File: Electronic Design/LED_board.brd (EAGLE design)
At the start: 49.2 x 29.2 mm, 12 parts

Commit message: Adding resistor values
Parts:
- R1, R2, R3, R4, R5: value (none) -> 270E
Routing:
- net N$3: track 27.1 -> 25.6 mm
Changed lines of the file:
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@@
 <attribute name="VALUE" x="6.8834" y="26.0604" size="1.27" layer="27" ratio="10" rot="R90"/>
 </element>
-<element name="R1" library="resistor" package="R0805" value="" x="35.56" y="7.62"/>
-<element name="R2" library="resistor" package="R0805" value="" x="35.56" y="15.24"/>
-<element name="R3" library="resistor" package="R0805" value="" x="35.56" y="22.86"/>
-<element name="R4" library="resistor" package="R0805" value="" x="20.32" y="16.51" rot="R90"/>
-<element name="R5" library="resistor" package="R0805" value="" x="12.7" y="16.51" rot="R90"/>
+<element name="R1" library="resistor" package="R0805" value="270E" x="35.56" y="7.62"/>
+<element name="R2" library="resistor" package="R0805" value="270E" x="35.56" y="15.24"/>
+<element name="R3" library="resistor" package="R0805" value="270E" x="35.56" y="22.86"/>
+<element name="R4" library="resistor" package="R0805" value="270E" x="20.32" y="16.51" rot="R90"/>
+<element name="R5" library="resistor" package="R0805" value="270E" x="12.7" y="16.51" rot="R90"/>
 </elements>
 <signals>
@@
 <contactref element="R3" pad="1"/>
 <contactref element="JP1" pad="3"/>
-<wire x1="22.86" y1="3.81" x2="22.86" y2="16.51" width="0.8128" layer="1"/>
-<wire x1="22.86" y1="16.51" x2="29.21" y2="22.86" width="0.8128" layer="1"/>
-<wire x1="29.21" y1="22.86" x2="34.61" y2="22.86" width="0.8128" layer="1"/>
+<wire x1="22.86" y1="3.81" x2="22.86" y2="13.97" width="0.8128" layer="1"/>
+<wire x1="22.86" y1="13.97" x2="31.75" y2="22.86" width="0.8128" layer="1"/>
+<wire x1="31.75" y1="22.86" x2="34.61" y2="22.86" width="0.8128" layer="1"/>
 </signal>
 <signal name="N$5">

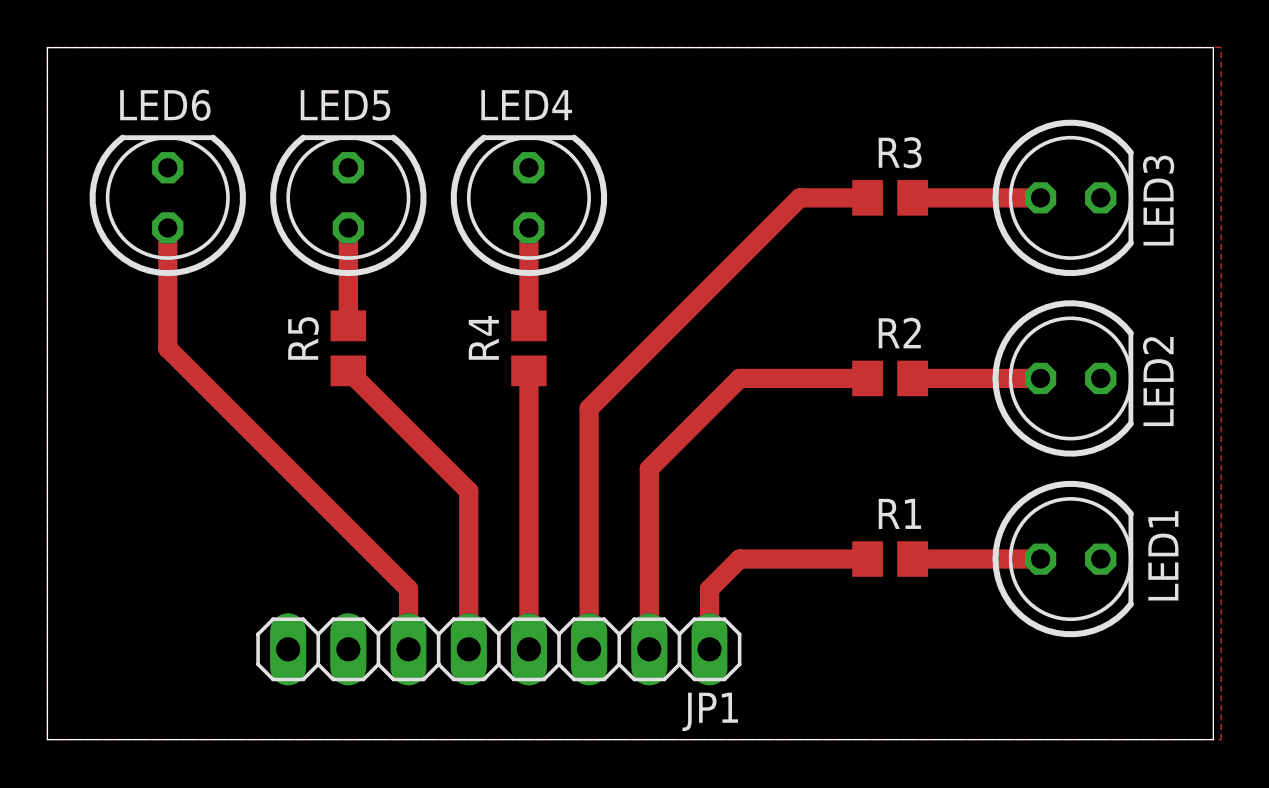
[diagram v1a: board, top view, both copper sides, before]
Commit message: added drill holes
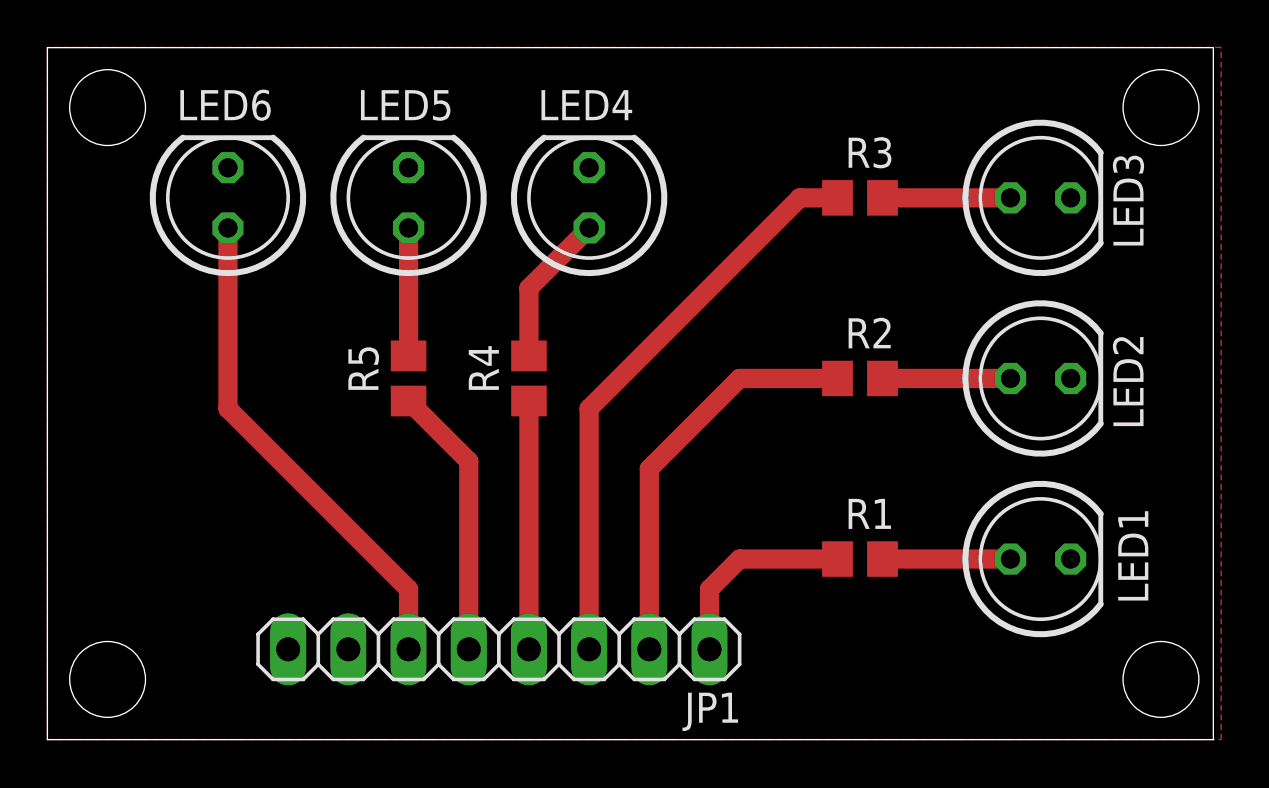
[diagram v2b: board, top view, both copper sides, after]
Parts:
- moved R5 2.84 mm to (15.2, 15.2)
- moved LED5 2.54 mm to (15.2, 22.9)
- moved LED6 2.54 mm to (7.62, 22.9)
- moved LED4 2.54 mm to (22.9, 22.9)
- moved LED1 1.27 mm to (41.9, 7.62)
- moved LED2 1.27 mm to (41.9, 15.2)
- moved LED3 1.27 mm to (41.9, 22.9)
- moved R1 1.27 mm to (34.3, 7.62)
- moved R2 1.27 mm to (34.3, 15.2)
- moved R3 1.27 mm to (34.3, 22.9)
- moved R4 1.27 mm to (20.3, 15.2)
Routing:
- net N$6: track 13.9 -> 11.5 mm
- net N$8: track 4.13 -> 6.45 mm
- net N$4: track 11.8 -> 10.5 mm
- net N$7: track 4.13 -> 5.40 mm
- net N$3: track 25.6 -> 24.3 mm
- net N$2: track 18.4 -> 17.1 mm
- net N$1: track 9.74 -> 8.47 mm
- net N$5: track 22.0 -> 20.9 mm
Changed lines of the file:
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@@
 <layer number="43" name="vRestrict" color="2" fill="10" visible="yes" active="yes"/>
 <layer number="44" name="Drills" color="7" fill="1" visible="no" active="yes"/>
-<layer number="45" name="Holes" color="7" fill="1" visible="no" active="yes"/>
+<layer number="45" name="Holes" color="7" fill="1" visible="yes" active="yes"/>
 <layer number="46" name="Milling" color="3" fill="1" visible="no" active="yes"/>
 <layer number="47" name="Measures" color="7" fill="1" visible="no" active="yes"/>
@@
 <wire x1="49.2" y1="29.2" x2="0" y2="29.2" width="0" layer="20"/>
 <wire x1="0" y1="29.2" x2="0" y2="0" width="0" layer="20"/>
+<hole x="46.99" y="26.67" drill="3.2"/>
+<hole x="46.99" y="2.54" drill="3.2"/>
+<hole x="2.54" y="2.54" drill="3.2"/>
+<hole x="2.54" y="26.67" drill="3.2"/>
 </plain>
 <attributes>
@@
 <elements>
 <element name="JP1" library="pinhead" package="1X08" value="" x="19.05" y="3.81" rot="R180"/>
-<element name="LED1" library="led" package="LED5MM" value="" x="43.18" y="7.62" smashed="yes">
-<attribute name="NAME" x="47.7266" y="5.715" size="1.27" layer="25" ratio="10" rot="R90"/>
-<attribute name="VALUE" x="46.3804" y="5.8166" size="1.27" layer="27" ratio="10"/>
-</element>
-<element name="LED2" library="led" package="LED5MM" value="" x="43.18" y="15.24" smashed="yes">
-<attribute name="NAME" x="46.2534" y="17.145" size="1.27" layer="25" ratio="10" rot="R270"/>
-<attribute name="VALUE" x="46.3804" y="13.4366" size="1.27" layer="27" ratio="10"/>
-</element>
-<element name="LED3" library="led" package="LED5MM" value="" x="43.18" y="22.86" smashed="yes">
-<attribute name="NAME" x="46.2534" y="24.765" size="1.27" layer="25" ratio="10" rot="R270"/>
-<attribute name="VALUE" x="46.3804" y="21.0566" size="1.27" layer="27" ratio="10"/>
-</element>
-<element name="LED4" library="led" package="LED5MM" value="" x="20.32" y="22.86" smashed="yes" rot="R90">
-<attribute name="NAME" x="22.225" y="27.4066" size="1.27" layer="25" ratio="10" rot="R180"/>
-<attribute name="VALUE" x="22.1234" y="26.0604" size="1.27" layer="27" ratio="10" rot="R90"/>
-</element>
-<element name="LED5" library="led" package="LED5MM" value="" x="12.7" y="22.86" smashed="yes" rot="R90">
-<attribute name="NAME" x="14.605" y="27.4066" size="1.27" layer="25" ratio="10" rot="R180"/>
-<attribute name="VALUE" x="14.5034" y="26.0604" size="1.27" layer="27" ratio="10" rot="R90"/>
-</element>
-<element name="LED6" library="led" package="LED5MM" value="" x="5.08" y="22.86" smashed="yes" rot="R90">
-<attribute name="NAME" x="6.985" y="27.4066" size="1.27" layer="25" ratio="10" rot="R180"/>
-<attribute name="VALUE" x="6.8834" y="26.0604" size="1.27" layer="27" ratio="10" rot="R90"/>
-</element>
-<element name="R1" library="resistor" package="R0805" value="270E" x="35.56" y="7.62"/>
-<element name="R2" library="resistor" package="R0805" value="270E" x="35.56" y="15.24"/>
-<element name="R3" library="resistor" package="R0805" value="270E" x="35.56" y="22.86"/>
-<element name="R4" library="resistor" package="R0805" value="270E" x="20.32" y="16.51" rot="R90"/>
-<element name="R5" library="resistor" package="R0805" value="270E" x="12.7" y="16.51" rot="R90"/>
+<element name="LED1" library="led" package="LED5MM" value="" x="41.91" y="7.62" smashed="yes">
+<attribute name="NAME" x="46.4566" y="5.715" size="1.27" layer="25" ratio="10" rot="R90"/>
+<attribute name="VALUE" x="45.1104" y="5.8166" size="1.27" layer="27" ratio="10"/>
+</element>
+<element name="LED2" library="led" package="LED5MM" value="" x="41.91" y="15.24" smashed="yes">
+<attribute name="NAME" x="44.9834" y="17.145" size="1.27" layer="25" ratio="10" rot="R270"/>
+<attribute name="VALUE" x="45.1104" y="13.4366" size="1.27" layer="27" ratio="10"/>
+</element>
+<element name="LED3" library="led" package="LED5MM" value="" x="41.91" y="22.86" smashed="yes">
+<attribute name="NAME" x="44.9834" y="24.765" size="1.27" layer="25" ratio="10" rot="R270"/>
+<attribute name="VALUE" x="45.1104" y="21.0566" size="1.27" layer="27" ratio="10"/>
+</element>
+<element name="LED4" library="led" package="LED5MM" value="" x="22.86" y="22.86" smashed="yes" rot="R90">
+<attribute name="NAME" x="24.765" y="27.4066" size="1.27" layer="25" ratio="10" rot="R180"/>
+<attribute name="VALUE" x="24.6634" y="26.0604" size="1.27" layer="27" ratio="10" rot="R90"/>
+</element>
+<element name="LED5" library="led" package="LED5MM" value="" x="15.24" y="22.86" smashed="yes" rot="R90">
+<attribute name="NAME" x="17.145" y="27.4066" size="1.27" layer="25" ratio="10" rot="R180"/>
+<attribute name="VALUE" x="17.0434" y="26.0604" size="1.27" layer="27" ratio="10" rot="R90"/>
+</element>
+<element name="LED6" library="led" package="LED5MM" value="" x="7.62" y="22.86" smashed="yes" rot="R90">
+<attribute name="NAME" x="9.525" y="27.4066" size="1.27" layer="25" ratio="10" rot="R180"/>
+<attribute name="VALUE" x="9.4234" y="26.0604" size="1.27" layer="27" ratio="10" rot="R90"/>
+</element>
+<element name="R1" library="resistor" package="R0805" value="270E" x="34.29" y="7.62"/>
+<element name="R2" library="resistor" package="R0805" value="270E" x="34.29" y="15.24"/>
+<element name="R3" library="resistor" package="R0805" value="270E" x="34.29" y="22.86"/>
+<element name="R4" library="resistor" package="R0805" value="270E" x="20.32" y="15.24" rot="R90"/>
+<element name="R5" library="resistor" package="R0805" value="270E" x="15.24" y="15.24" rot="R90"/>
 </elements>
 <signals>
@@
 <wire x1="27.94" y1="3.81" x2="27.94" y2="6.35" width="0.8128" layer="1"/>
 <wire x1="27.94" y1="6.35" x2="29.21" y2="7.62" width="0.8128" layer="1"/>
-<wire x1="29.21" y1="7.62" x2="34.61" y2="7.62" width="0.8128" layer="1"/>
+<wire x1="29.21" y1="7.62" x2="33.34" y2="7.62" width="0.8128" layer="1"/>
 </signal>
 <signal name="N$2">
@@
 <wire x1="25.4" y1="3.81" x2="25.4" y2="11.43" width="0.8128" layer="1"/>
 <wire x1="25.4" y1="11.43" x2="29.21" y2="15.24" width="0.8128" layer="1"/>
-<wire x1="29.21" y1="15.24" x2="34.61" y2="15.24" width="0.8128" layer="1"/>
+<wire x1="29.21" y1="15.24" x2="33.34" y2="15.24" width="0.8128" layer="1"/>
 </signal>
 <signal name="N$3">
@@
 <wire x1="22.86" y1="3.81" x2="22.86" y2="13.97" width="0.8128" layer="1"/>
 <wire x1="22.86" y1="13.97" x2="31.75" y2="22.86" width="0.8128" layer="1"/>
-<wire x1="31.75" y1="22.86" x2="34.61" y2="22.86" width="0.8128" layer="1"/>
+<wire x1="31.75" y1="22.86" x2="33.34" y2="22.86" width="0.8128" layer="1"/>
 </signal>
 <signal name="N$5">
@@
 <contactref element="LED6" pad="A"/>
 <wire x1="15.24" y1="3.81" x2="15.24" y2="6.35" width="0.8128" layer="1"/>
-<wire x1="15.24" y1="6.35" x2="5.08" y2="16.51" width="0.8128" layer="1"/>
-<wire x1="5.08" y1="16.51" x2="5.08" y2="21.59" width="0.8128" layer="1"/>
+<wire x1="15.24" y1="6.35" x2="7.62" y2="13.97" width="0.8128" layer="1"/>
+<wire x1="7.62" y1="13.97" x2="7.62" y2="21.59" width="0.8128" layer="1"/>
 </signal>
 <signal name="N$6">
 <contactref element="R5" pad="1"/>
 <contactref element="JP1" pad="5"/>
-<wire x1="17.78" y1="3.81" x2="17.78" y2="10.48" width="0.8128" layer="1"/>
-<wire x1="17.78" y1="10.48" x2="12.7" y2="15.56" width="0.8128" layer="1"/>
+<wire x1="17.78" y1="3.81" x2="17.78" y2="11.75" width="0.8128" layer="1"/>
+<wire x1="17.78" y1="11.75" x2="15.24" y2="14.29" width="0.8128" layer="1"/>
 </signal>
 <signal name="N$4">
 <contactref element="R4" pad="1"/>
 <contactref element="JP1" pad="4"/>
-<wire x1="20.32" y1="3.81" x2="20.32" y2="15.56" width="0.8128" layer="1"/>
+<wire x1="20.32" y1="3.81" x2="20.32" y2="14.29" width="0.8128" layer="1"/>
 </signal>
 <signal name="GND">
@@
 <contactref element="R5" pad="2"/>
 <contactref element="LED5" pad="A"/>
-<wire x1="12.7" y1="17.46" x2="12.7" y2="21.59" width="0.8128" layer="1"/>
+<wire x1="15.24" y1="16.19" x2="15.24" y2="21.59" width="0.8128" layer="1"/>
 </signal>
 <signal name="N$8">
 <contactref element="R4" pad="2"/>
 <contactref element="LED4" pad="A"/>
-<wire x1="20.32" y1="17.46" x2="20.32" y2="21.59" width="0.8128" layer="1"/>
+<wire x1="20.32" y1="16.19" x2="20.32" y2="19.05" width="0.8128" layer="1"/>
+<wire x1="20.32" y1="19.05" x2="22.86" y2="21.59" width="0.8128" layer="1"/>
 </signal>
 <signal name="N$9">
 <contactref element="R3" pad="2"/>
 <contactref element="LED3" pad="A"/>
-<wire x1="36.51" y1="22.86" x2="41.91" y2="22.86" width="0.8128" layer="1"/>
+<wire x1="35.24" y1="22.86" x2="40.64" y2="22.86" width="0.8128" layer="1"/>
 </signal>
 <signal name="N$10">
 <contactref element="R2" pad="2"/>
 <contactref element="LED2" pad="A"/>
-<wire x1="36.51" y1="15.24" x2="41.91" y2="15.24" width="0.8128" layer="1"/>
+<wire x1="35.24" y1="15.24" x2="40.64" y2="15.24" width="0.8128" layer="1"/>
 </signal>
 <signal name="N$11">
 <contactref element="R1" pad="2"/>
 <contactref element="LED1" pad="A"/>
-<wire x1="36.51" y1="7.62" x2="41.91" y2="7.62" width="0.8128" layer="1"/>
+<wire x1="35.24" y1="7.62" x2="40.64" y2="7.62" width="0.8128" layer="1"/>
 </signal>
 </signals>

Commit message: changing resistors to 1206 size
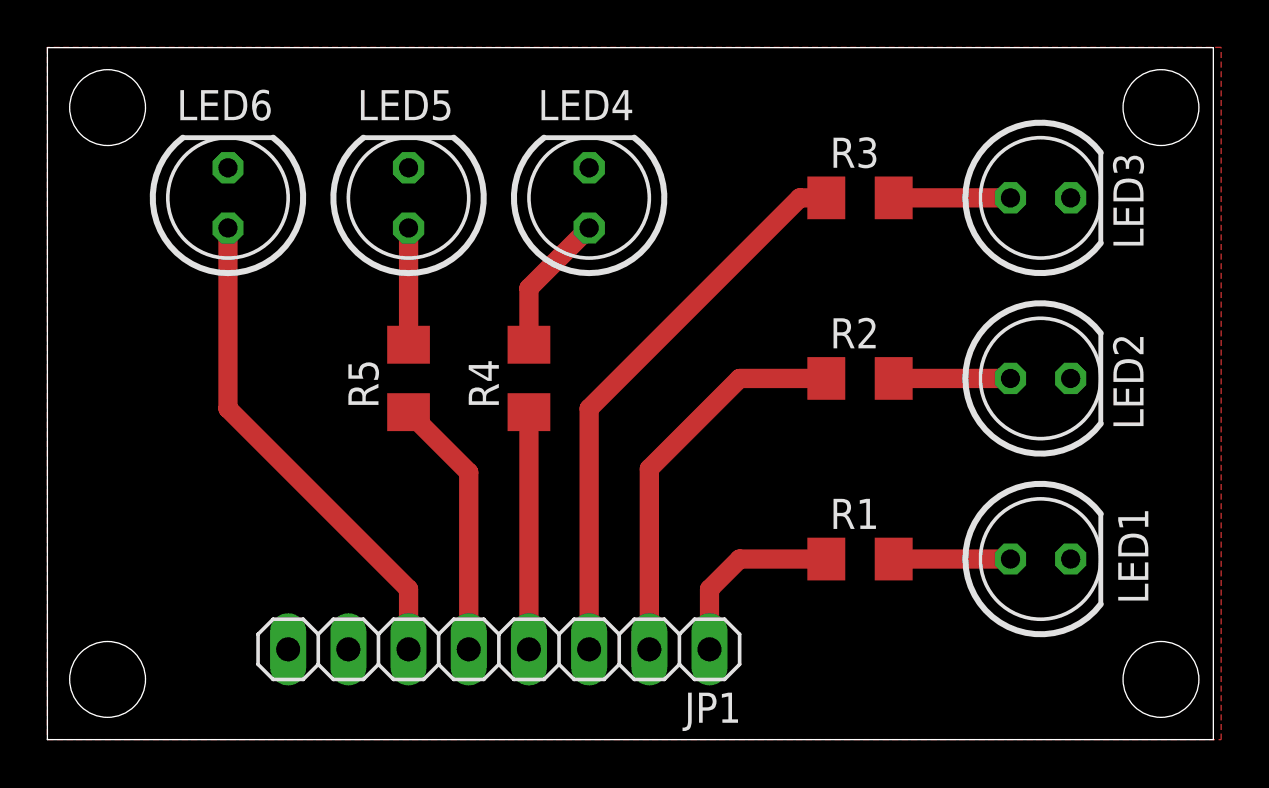
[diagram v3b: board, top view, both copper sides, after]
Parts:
- R1, R2, R3, R4, R5: device resistor:R0805 -> resistor:R1206
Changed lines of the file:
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@@
 <attribute name="VALUE" x="9.4234" y="26.0604" size="1.27" layer="27" ratio="10" rot="R90"/>
 </element>
-<element name="R1" library="resistor" package="R0805" value="270E" x="34.29" y="7.62"/>
-<element name="R2" library="resistor" package="R0805" value="270E" x="34.29" y="15.24"/>
-<element name="R3" library="resistor" package="R0805" value="270E" x="34.29" y="22.86"/>
-<element name="R4" library="resistor" package="R0805" value="270E" x="20.32" y="15.24" rot="R90"/>
-<element name="R5" library="resistor" package="R0805" value="270E" x="15.24" y="15.24" rot="R90"/>
+<element name="R1" library="resistor" package="R1206" value="270E" x="34.29" y="7.62"/>
+<element name="R2" library="resistor" package="R1206" value="270E" x="34.29" y="15.24"/>
+<element name="R3" library="resistor" package="R1206" value="270E" x="34.29" y="22.86"/>
+<element name="R4" library="resistor" package="R1206" value="270E" x="20.32" y="15.24" rot="R90"/>
+<element name="R5" library="resistor" package="R1206" value="270E" x="15.24" y="15.24" rot="R90"/>
 </elements>
 <signals>
@@
 <wire x1="27.94" y1="3.81" x2="27.94" y2="6.35" width="0.8128" layer="1"/>
 <wire x1="27.94" y1="6.35" x2="29.21" y2="7.62" width="0.8128" layer="1"/>
-<wire x1="29.21" y1="7.62" x2="33.34" y2="7.62" width="0.8128" layer="1"/>
+<wire x1="29.21" y1="7.62" x2="32.868" y2="7.62" width="0.8128" layer="1"/>
 </signal>
 <signal name="N$2">
@@
 <wire x1="25.4" y1="3.81" x2="25.4" y2="11.43" width="0.8128" layer="1"/>
 <wire x1="25.4" y1="11.43" x2="29.21" y2="15.24" width="0.8128" layer="1"/>
-<wire x1="29.21" y1="15.24" x2="33.34" y2="15.24" width="0.8128" layer="1"/>
+<wire x1="29.21" y1="15.24" x2="32.868" y2="15.24" width="0.8128" layer="1"/>
 </signal>
 <signal name="N$3">
@@
 <wire x1="22.86" y1="3.81" x2="22.86" y2="13.97" width="0.8128" layer="1"/>
 <wire x1="22.86" y1="13.97" x2="31.75" y2="22.86" width="0.8128" layer="1"/>
-<wire x1="31.75" y1="22.86" x2="33.34" y2="22.86" width="0.8128" layer="1"/>
+<wire x1="31.75" y1="22.86" x2="32.868" y2="22.86" width="0.8128" layer="1"/>
 </signal>
 <signal name="N$5">
@@
 <contactref element="R5" pad="1"/>
 <contactref element="JP1" pad="5"/>
-<wire x1="17.78" y1="3.81" x2="17.78" y2="11.75" width="0.8128" layer="1"/>
-<wire x1="17.78" y1="11.75" x2="15.24" y2="14.29" width="0.8128" layer="1"/>
+<wire x1="17.78" y1="3.81" x2="17.78" y2="11.278" width="0.8128" layer="1"/>
+<wire x1="17.78" y1="11.278" x2="15.24" y2="13.818" width="0.8128" layer="1"/>
 </signal>
 <signal name="N$4">
 <contactref element="R4" pad="1"/>
 <contactref element="JP1" pad="4"/>
-<wire x1="20.32" y1="3.81" x2="20.32" y2="14.29" width="0.8128" layer="1"/>
+<wire x1="20.32" y1="3.81" x2="20.32" y2="13.818" width="0.8128" layer="1"/>
 </signal>
 <signal name="GND">
@@
 <contactref element="R5" pad="2"/>
 <contactref element="LED5" pad="A"/>
-<wire x1="15.24" y1="16.19" x2="15.24" y2="21.59" width="0.8128" layer="1"/>
+<wire x1="15.24" y1="16.662" x2="15.24" y2="21.59" width="0.8128" layer="1"/>
 </signal>
 <signal name="N$8">
 <contactref element="R4" pad="2"/>
 <contactref element="LED4" pad="A"/>
-<wire x1="20.32" y1="16.19" x2="20.32" y2="19.05" width="0.8128" layer="1"/>
+<wire x1="20.32" y1="16.662" x2="20.32" y2="19.05" width="0.8128" layer="1"/>
 <wire x1="20.32" y1="19.05" x2="22.86" y2="21.59" width="0.8128" layer="1"/>
 </signal>
@@
 <contactref element="R3" pad="2"/>
 <contactref element="LED3" pad="A"/>
-<wire x1="35.24" y1="22.86" x2="40.64" y2="22.86" width="0.8128" layer="1"/>
+<wire x1="35.712" y1="22.86" x2="40.64" y2="22.86" width="0.8128" layer="1"/>
 </signal>
 <signal name="N$10">
 <contactref element="R2" pad="2"/>
 <contactref element="LED2" pad="A"/>
-<wire x1="35.24" y1="15.24" x2="40.64" y2="15.24" width="0.8128" layer="1"/>
+<wire x1="35.712" y1="15.24" x2="40.64" y2="15.24" width="0.8128" layer="1"/>
 </signal>
 <signal name="N$11">
 <contactref element="R1" pad="2"/>
 <contactref element="LED1" pad="A"/>
-<wire x1="35.24" y1="7.62" x2="40.64" y2="7.62" width="0.8128" layer="1"/>
+<wire x1="35.712" y1="7.62" x2="40.64" y2="7.62" width="0.8128" layer="1"/>
 </signal>
 </signals>
